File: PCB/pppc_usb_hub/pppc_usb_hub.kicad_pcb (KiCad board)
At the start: 2 copper layers, 69.6 x 48 mm, 83 parts, among them J1 USB_C_Signal, J2 USB_C_Signal, J3 USB_A_1, J4 USB_A_2, J5 USB_A_3, J6 Con_Relay, J7 Conn_UART, J8 Conn_Debug, K1 Relay, Q1 DMG2305UX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

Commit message: Rev 2
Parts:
- removed REF** (x2): MountingHole_2.2mm_M2_ISO7380_Pad, MountingHole:MountingHole_2.2mm_M2_ISO7380_Pad
- added G***: LOGO, LOGO, F.Cu at (163.7, 98.7)
- C1, C10, C11, C15, C16, C17, C18, C19, C2, C20, C23, C24, C25, C3, C4, C5, C6, C7, C8, C9: footprint Capacitor_SMD:C_0201_0603Metric -> Capacitor_SMD:C_0603_1608Metric
- D2, D3, D4, D5, D6: footprint LED_SMD:LED_0201_0603Metric -> LED_SMD:LED_0603_1608Metric
- R1, R10, R11, R12, R13, R14, R15, R16, R17, R18, R19, R2, R20, R21, R22, R3, R4, R5, R6, R7, R8, R9: footprint Resistor_SMD:R_0201_0603Metric -> Resistor_SMD:R_0603_1608Metric
- SW4: footprint PCBLIB_SW-SMD_L6.0-W3.3-LS8.0_2024-05-19:SW-SMD_L6.0-W3.3-LS8.0 -> PCBLIB_SW-SMD_GT-TC020B-H035-L05_2024-05-21:SW-SMD_GT-TC020B-H035-L05
- moved SW4 82.6 mm to (177.8, 83.2)
- moved R22 81.7 mm to (177.8, 86.1)
- moved J7 59.5 mm to (163.8, 109.5), turned to 0 degrees
- moved R10 57.7 mm to (137.4, 104.5), turned to -90 degrees
- moved R8 47.5 mm to (156.3, 108.1)
- moved R7 47.5 mm to (141.3, 108.1)
- moved R6 47.2 mm to (123.3, 108.1)
- moved R19 47.0 mm to (175.3, 90.6), turned to 90 degrees
- moved R3 46.6 mm to (158.8, 111.6), turned to 90 degrees
- moved R2 46.5 mm to (143.8, 111.6), turned to 90 degrees
- moved U2 46.2 mm to (141.4, 111.1), turned to -90 degrees
- moved U3 46.2 mm to (156.4, 111.1), turned to -90 degrees
- moved R1 46.2 mm to (125.8, 111.6), turned to 90 degrees
- moved U1 45.8 mm to (123.4, 111.1), turned to -90 degrees
- moved C3 45.8 mm to (154.0, 110.6), turned to -90 degrees
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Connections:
- U4 pad 1: /MCU_DN -> /DN3
- U4 pad 13: /DN2 -> /DN1
- U4 pad 14: /DP2 -> /DP1
- U4 pad 15: /DN3 -> /DN2
- U4 pad 16: /DP3 -> /DP2
- U4 pad 2: /MCU_DP -> /DP3
- U4 pad 3: /DN1 -> /MCU_DN
- U4 pad 4: /DP1 -> /MCU_DP
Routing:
- net GND: track 13.8 -> 90.8 mm, vias 141 -> 118
- net /NRST: track 22.1 -> 58.5 mm
- net /BOOT0: track 22.6 -> 58.5 mm
- net /VBUS: track 225.6 -> 191.0 mm, vias 8 -> 13
- net /SWDIO: track 54.5 -> 22.4 mm
- net /COM: track 23.7 -> 0.00 mm, vias 0 -> 16
- net /UART_RX: track 26.4 -> 49.8 mm
- net /SWCLK: track 47.6 -> 26.0 mm
- net /EN2: track 14.6 -> 36.2 mm, vias 2 -> 5
- net /EN3: track 26.5 -> 46.1 mm, vias 2 -> 4
- net /UART_TX: track 28.4 -> 44.6 mm
- net VEXT: track 15.5 -> 0.00 mm
- net VUSB: track 13.5 -> 27.0 mm, vias 0 -> 5
- net /VBUS2: track 31.7 -> 21.0 mm, vias 2 -> 0
- net /VBUS3: track 31.1 -> 20.7 mm, vias 1 -> 0
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- added copper zone on F.Cu, net +3.3V
- added copper zone on B.Cu, net /COM
- added copper zone on F.Cu, net /COM
- added copper zone on In1.Cu, net /COM
- added copper zone on In2.Cu, net /COM
- added copper zone on B.Cu, net /NC
- added copper zone on F.Cu, net /NC
- added copper zone on In1.Cu, net /NC
- added copper zone on In2.Cu, net /NC
- added copper zone on B.Cu, net /NO
- added copper zone on F.Cu, net /NO
- added copper zone on In1.Cu, net /NO
- added copper zone on In2.Cu, net /NO
- added copper zone on F.Cu, net /VBUS
- added copper zone on In2.Cu, net /VBUS
- added copper zone on In1.Cu, net GND
- added copper zone on In2.Cu, net GND
- added copper zone on F.Cu, net VEXT
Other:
- board size 69.6 x 48 mm -> 79.6 x 48 mm
- copper layers 2 -> 4
- board text added: "NO_MCU"

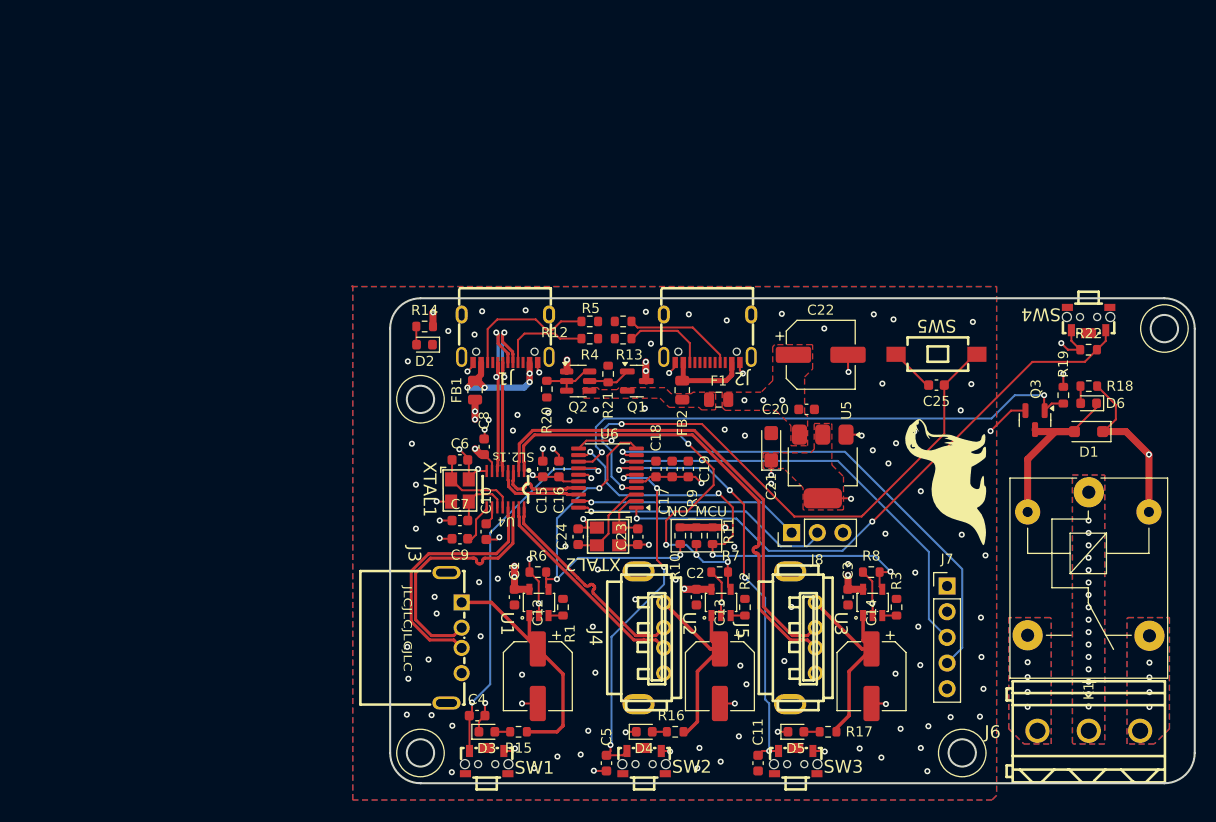
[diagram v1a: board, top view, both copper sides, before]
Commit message: Add firmware and update PCB to Rev 3
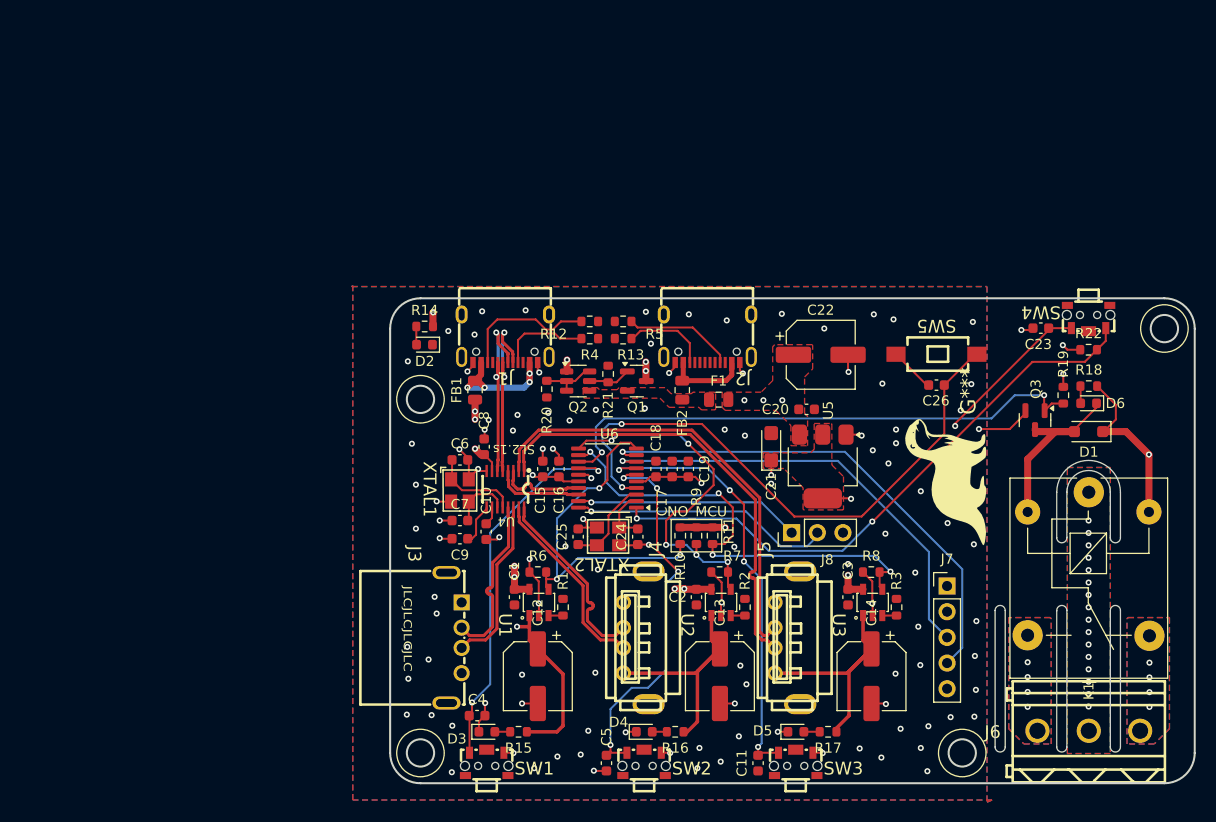
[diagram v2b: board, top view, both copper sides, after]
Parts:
- added C23: 0.1uF, Capacitor_SMD:C_0603_1608Metric, F.Cu at (173.1, 84.0)
- moved J4 1.50 mm to (133.0, 114.6), turned to 90 degrees
- moved J5 1.50 mm to (148.0, 114.6), turned to 90 degrees
- moved SW4 0.20 mm to (177.8, 83.0)
- moved SW1 0.17 mm to (118.2, 127.0)
- moved SW2 0.17 mm to (133.8, 127.0)
- moved SW3 0.17 mm to (148.8, 127.0)
- renumbered C23 to C24, C24 to C25, C25 to C26
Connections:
- J3 pad 2: /DP1 -> /DN1
- J3 pad 3: /DN1 -> /DP1
- J4 pad 2: /DP2 -> /DN2
- J4 pad 3: /DN2 -> /DP2
- J5 pad 2: /DP3 -> /DN3
- J5 pad 3: /DN3 -> /DP3
- SW4 pad 2: GND -> +3.3V
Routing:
- net +3.3V: track 64.2 -> 93.3 mm, vias 5 -> 6
- net /DN1: track 25.3 -> 16.9 mm
- net /DP1: track 25.3 -> 16.9 mm
- net GND: track 90.8 -> 97.3 mm, vias 118 -> 112
- net /VBUS3: track 20.7 -> 23.8 mm
- net /VBUS2: track 21.0 -> 24.1 mm
- net /DN3: track 47.5 -> 44.7 mm
- net /DP3: track 47.5 -> 44.8 mm
- net /DP2: track 21.1 -> 19.0 mm
- net /DN2: track 21.1 -> 19.1 mm
- net /SW2: track 36.4 -> 38.4 mm
- net /VBUS1: track 25.5 -> 23.8 mm, vias 0 -> 1
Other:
- outline, holes or cut-outs redrawn
